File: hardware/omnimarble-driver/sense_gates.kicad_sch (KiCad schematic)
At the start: 46 parts, among them J6 RAIL-EMIT, J7 RAIL-RECV, J8 SPARE-JST, U10 ADS7042, U11 LM339, U12 LM339, U9 INA240A1

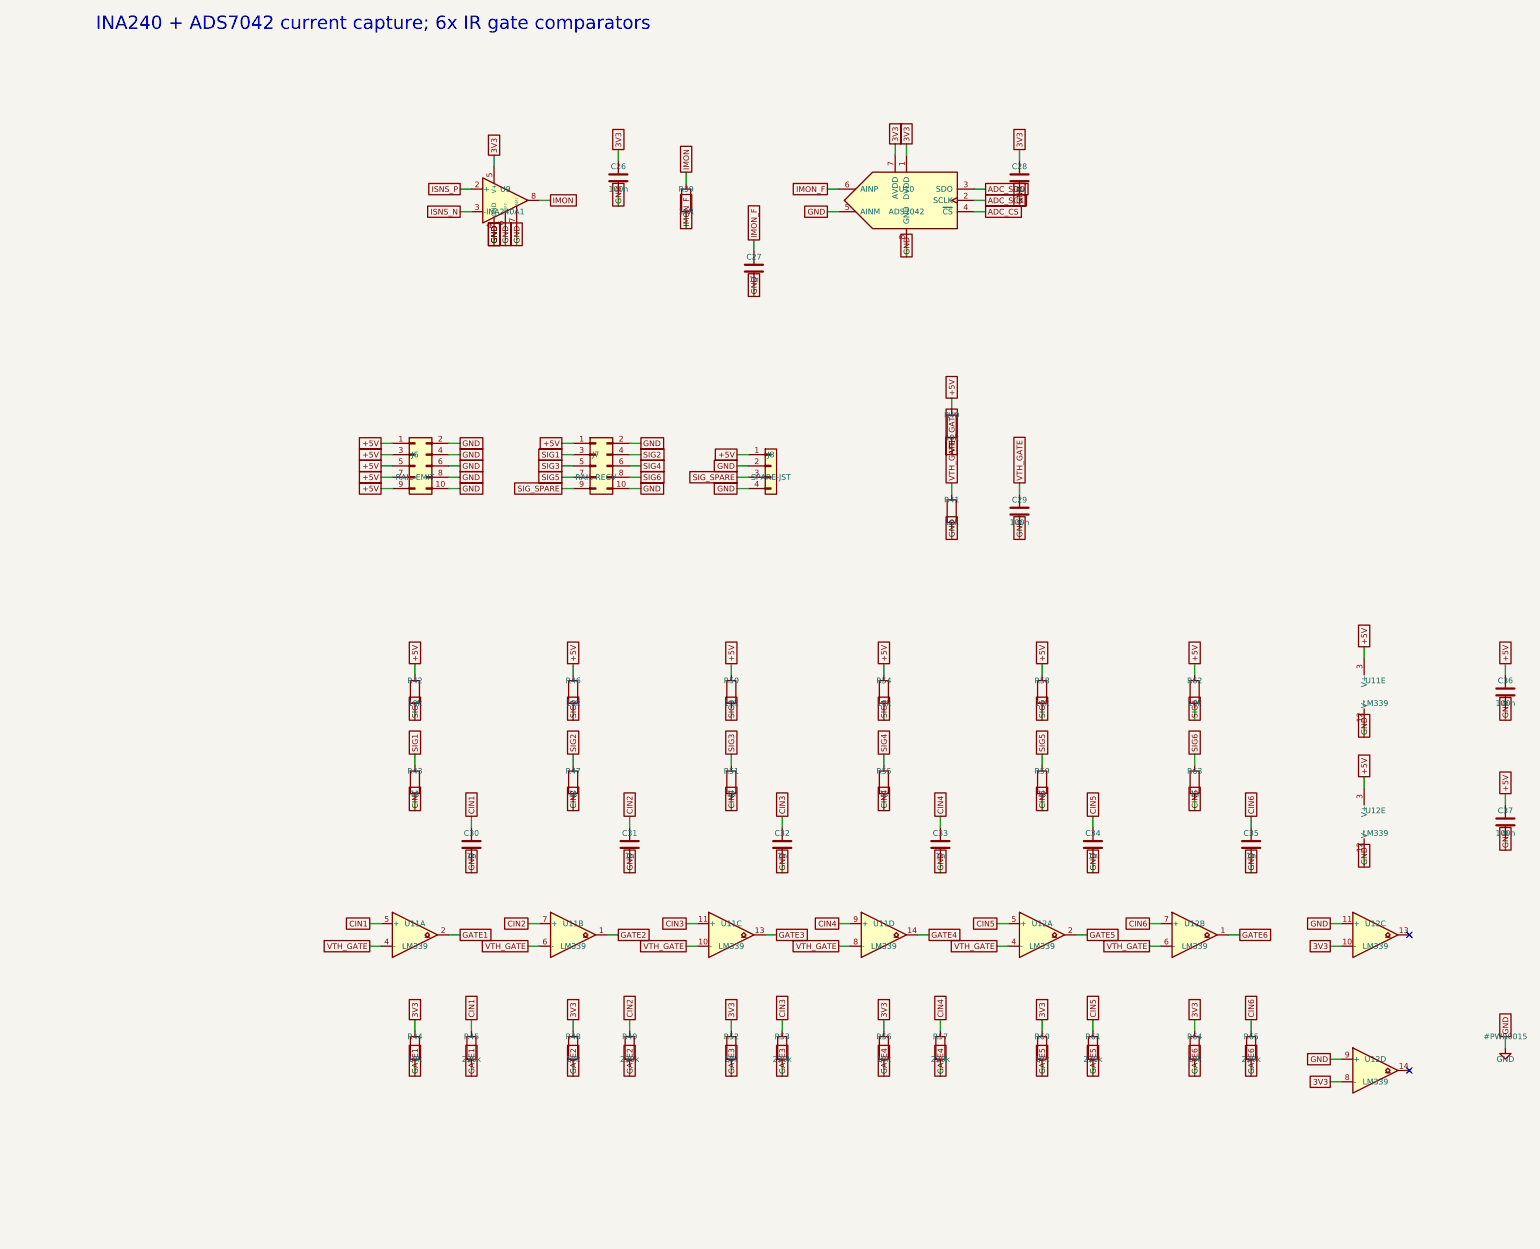
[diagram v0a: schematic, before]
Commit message: Address external design review: boost FB + OVP redesign, BOM freeze
Review findings accepted and fixed (each verified by machine check):

1. Boost feedback network was wrong (confirmed: as-drawn spanned
   54-68V with PWM inverted vs the comment). Redesigned: RT/RB/RJ =
   100k/10k/9.1k with the exact transfer function documented in the
   schematic and design-calcs.md. PWM=0 (MCU-dead state) commands
   55.0V; full PWM commands 18.7V (below the 24.5V converter floor).
   New calcs.py asserts both endpoints.
2. OVP tripped at 55.6V, not the claimed 63V (confirmed). Redesigned:
   CJ431 (+/-0.5%) + 100k/4.3k 1% -> 60.5V nominal, 59.1-62.0V across
   tolerances. Protection ladder asserted in calcs.py: 55V operating
   < 59.1V trip-min, 62.0V trip-max < 63V cap rating - 1V. Operating
   ceiling deliberately reduced 60->55V to keep the bands disjoint.
3. BOM/schematic controller split-brain: bom.csv was stale
   (pre-UC3843 swap); regenerated from parts.py. Both now UC3843B.
4. High-power placeholders now real orderable parts (LCSC-verified):
   47R/5W SQM cement C5807995, dump redesigned to 2x 100R/10W cement
   in series C216413 (no 20-25W part stocked on LCSC; 5.3s to <5V),
   50mR/3W 2512 C2994645, 63V/35V electrolytics C28241/C176666, 10uH
   Sunlord C79272, MINI fuses+Keystone 3568 holders, buzzer, Pico
   sockets/breakout headers. Single documented exception: the 6.8k/2W
   bleed (CRH2512J6K80E04Z) is marked ORDER-REVIEW because LCSC's
   search is uncrawlable - validate.py allowlists it visibly.
5. validate.py pulled forward from the fab phase: fails on unknown
   footprints, blank LCSC on machine-placed parts, missing Variant
   fields, and duplicate refs; generates per-variant gate-rail BOMs
   (bom_rail_emit/recv.csv). Caught two bad footprint names.
6. Paralleling constraints now on the schematic (same-lot FETs,
   symmetric copper, <25mm gate loops, driver return at shunt star).
7. Fail-safe defaults hardened: MCU_FIRE and FIRE_GATED get explicit
   pulldow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
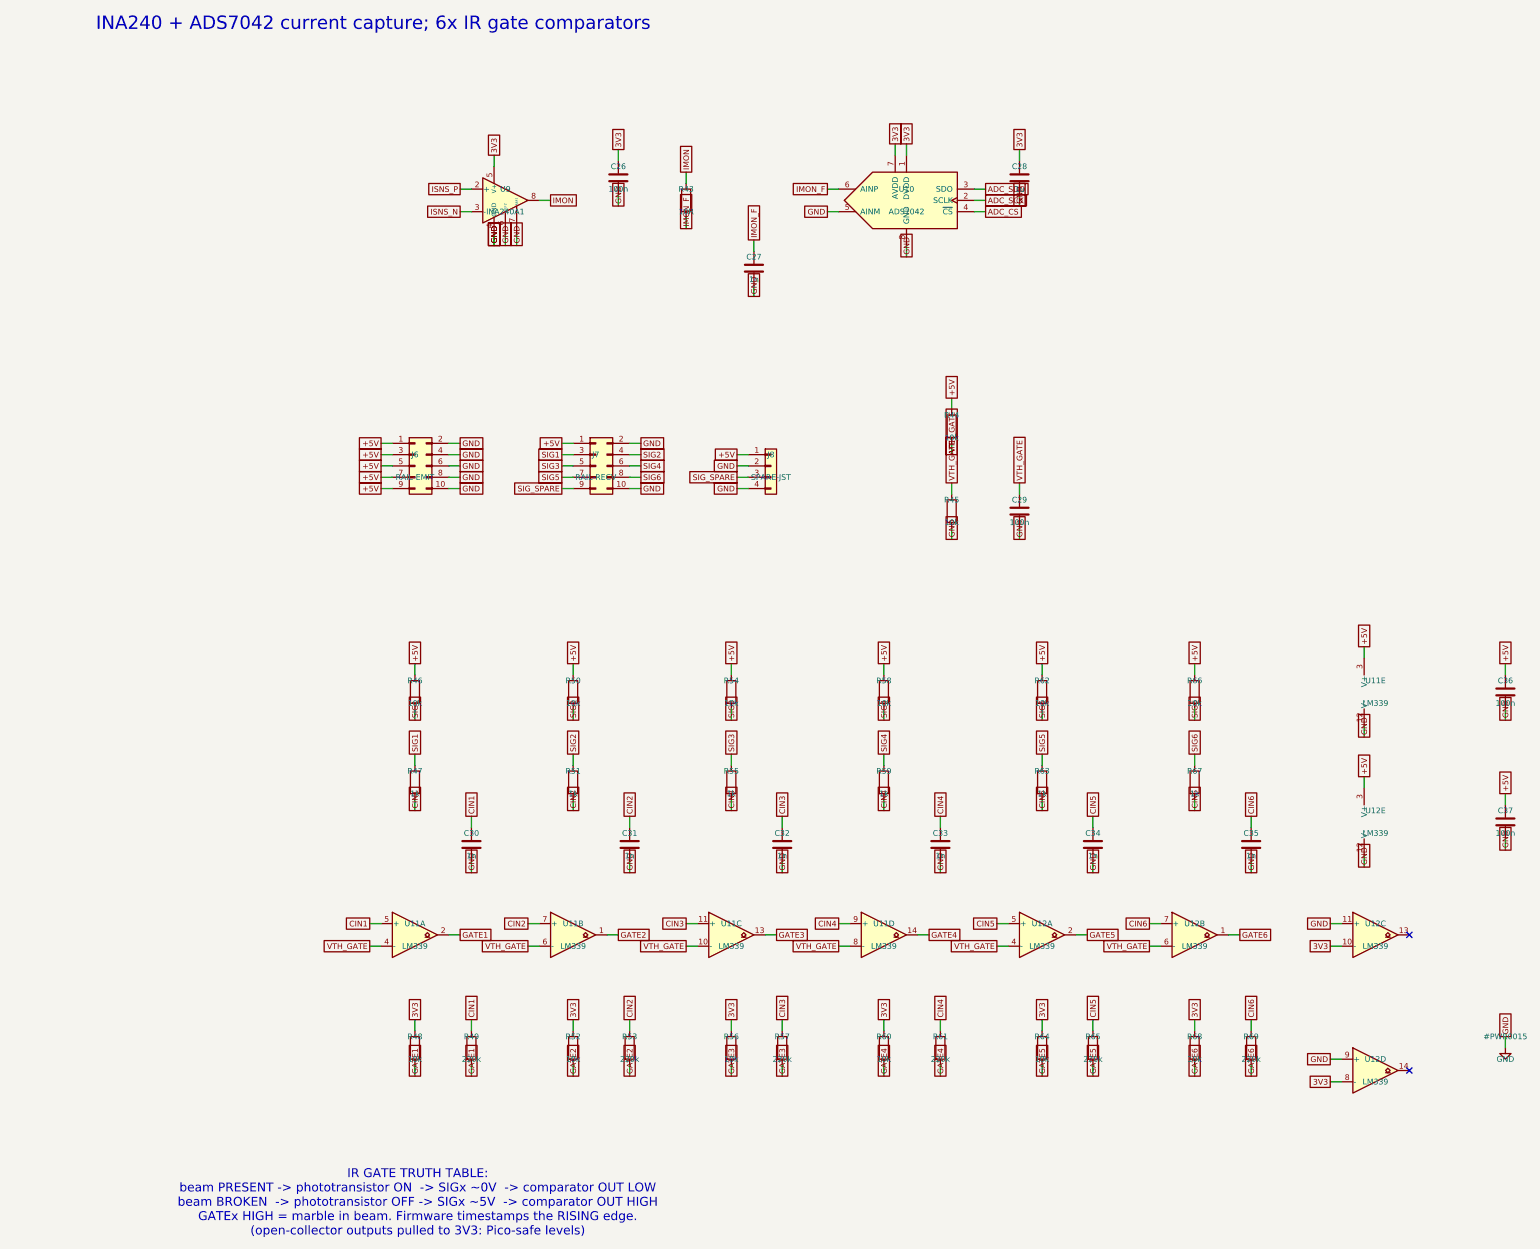
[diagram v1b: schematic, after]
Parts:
- removed R39: 10R, Resistor_SMD:R_0603_1608Metric, symbol Device:R
- removed R40, R41, R42: 10k, Resistor_SMD:R_0603_1608Metric, symbol Device:R
- added R66, R68: 10k, Resistor_SMD:R_0603_1608Metric, symbol Device:R
- added R67: 1k, Resistor_SMD:R_0603_1608Metric, symbol Device:R
- added R69: 220k, Resistor_SMD:R_0603_1608Metric, symbol Device:R
- R43: value 1k -> 10R; LCSC C21190 -> C22859
- R45: value 220k -> 10k; LCSC C22961 -> C25804
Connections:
- net +5V: now also R44.1, R66.1
- net 3V3: now also R68.1; no longer R44.1
- net CIN1: now also R47.2, R49.1; no longer R43.2, R45.1
- net CIN2: now also R51.2, R53.1; no longer R47.2, R49.1
- net CIN3: now also R55.2, R57.1; no longer R51.2, R53.1
- net CIN4: now also R59.2, R61.1; no longer R55.2, R57.1
- net CIN5: now also R63.2, R65.1; no longer R59.2, R61.1
- net CIN6: now also R67.2, R69.1; no longer R63.2, R65.1
- net GATE1: now also R48.2, R49.2; no longer R44.2, R45.2
- net GATE2: now also R52.2, R53.2; no longer R48.2, R49.2
- net GATE3: now also R56.2, R57.2; no longer R52.2, R53.2
- net GATE4: now also R60.2, R61.2; no longer R56.2, R57.2
- net GATE5: now also R64.2, R65.2; no longer R60.2, R61.2
- net GATE6: now also R68.2, R69.2; no longer R64.2, R65.2
- net GND: now also R45.2
- net IMON: now also R43.1
- net IMON_F: now also R43.2
- net SIG1: now also R46.2, R47.1; no longer R43.1
- net SIG2: now also R50.2, R51.1; no longer R46.2, R47.1
- net SIG3: now also R54.2, R55.1; no longer R50.2, R51.1
- net SIG4: now also R58.2, R59.1; no longer R54.2, R55.1
- net SIG5: now also R62.2, R63.1; no longer R58.2, R59.1
- net SIG6: now also R66.2, R67.1; no longer R62.2, R63.1
- net VTH_GATE: now also R44.2, R45.1
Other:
- note added: "IR GATE TRUTH TABLE: beam PRESENT -> phototransistor ON -> SIGx ~0V -> comparator OUT LOW beam BROKEN -> phototransistor OFF -> SIGx ~5V -> comparator OUT HIGH GATEx HIGH = marble in beam. Firmware timestamps the RISING edge. (open-collector outputs pulled to 3V3: Pico-safe levels)"
